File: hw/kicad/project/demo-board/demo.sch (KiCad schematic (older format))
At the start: 28 parts, among them J2 MICRO_SD_HINGE, P1 ESP_CONN, P2 ESP_CONN, P3 ESP_CONN, P4 PWR_CONN, P5 CONN_DISPLAY, P6 SD_LCD_CONN, SW1 KEY_FLASH, SW2 KEY_RST, U1 NCP1117ST33T3G, U2 ESP-12E

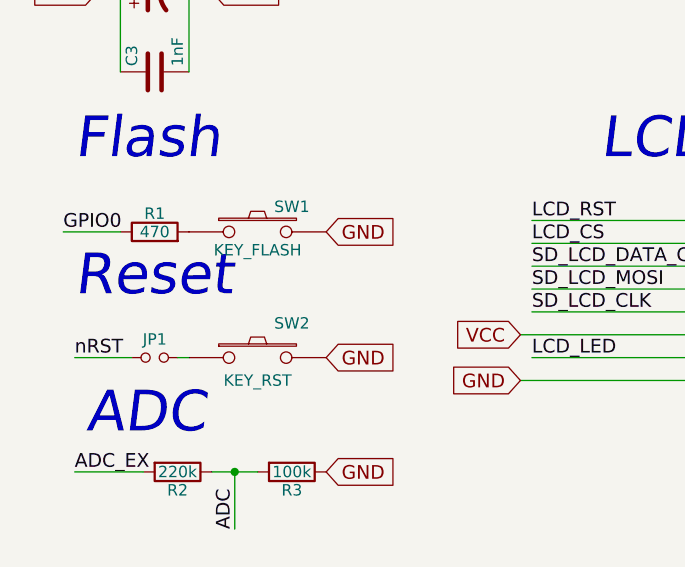
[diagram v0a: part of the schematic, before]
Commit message: Pushbuttons changed to the SMD type
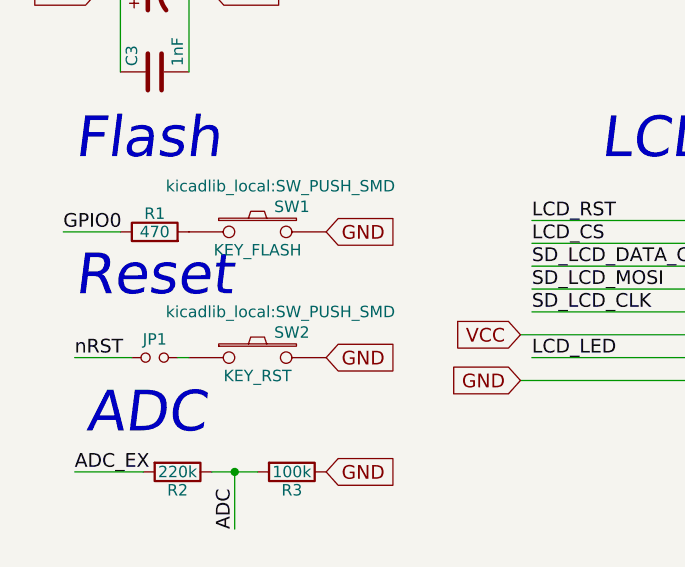
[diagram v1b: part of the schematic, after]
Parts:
- SW1, SW2: footprint Buttons_Switches_ThroughHole:SW_PUSH_SMALL -> kicadlib_local:SW_PUSH_SMD
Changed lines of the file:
@@
 LIBS:armory
 LIBS:display_local
+LIBS:open-project
 LIBS:demo-cache
 EELAYER 25 0
@@
 F 0 "SW1" H 1750 3760 50  0000 C CNN
 F 1 "KEY_FLASH" H 1600 3570 50  0000 C CNN
-F 2 "Buttons_Switches_ThroughHole:SW_PUSH_SMALL" H 1600 3650 50  0001 C CNN
+F 2 "kicadlib_local:SW_PUSH_SMD" H 1700 3850 50  0000 C CNN
 F 3 "" H 1600 3650 50  0000 C CNN
 	1    1600 3650
@@
 F 3 "" H 1150 4200 50  0000 C CNN
 	1    1150 4200
-	1    0    0    -1
-$EndComp
-$Comp
-L SW_PUSH SW2
-U 1 1 5673650D
-P 1600 4200
-F 0 "SW2" H 1750 4350 50  0000 C CNN
-F 1 "KEY_RST" H 1600 4100 50  0000 C CNN
-F 2 "Buttons_Switches_ThroughHole:SW_PUSH_SMALL" H 1600 4200 50  0001 C CNN
-F 3 "" H 1600 4200 50  0000 C CNN
-	1    1600 4200
 	1    0    0    -1
 $EndComp
@@
 	3200 6200 3200 7050
 Connection ~ 6150 6850
+$Comp
+L SW_PUSH SW2
+U 1 1 5673650D
+P 1600 4200
+F 0 "SW2" H 1750 4310 50  0000 C CNN
+F 1 "KEY_RST" H 1600 4120 50  0000 C CNN
+F 2 "kicadlib_local:SW_PUSH_SMD" H 1700 4400 50  0000 C CNN
+F 3 "" H 1600 4200 50  0000 C CNN
+	1    1600 4200
+	1    0    0    -1
+$EndComp
 $EndSCHEMATC
